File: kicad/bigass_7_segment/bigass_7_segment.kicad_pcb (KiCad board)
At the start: 2 copper layers, 30 x 94 mm, 37 parts, among them J1 Conn_01x02, J2 Conn_01x02, J3 Conn_01x02, J4 Conn_01x02, J5 Conn_01x01, J6 Conn_01x01, J7 Conn_01x01, J8 Conn_01x01, Q3 25V 1.5A

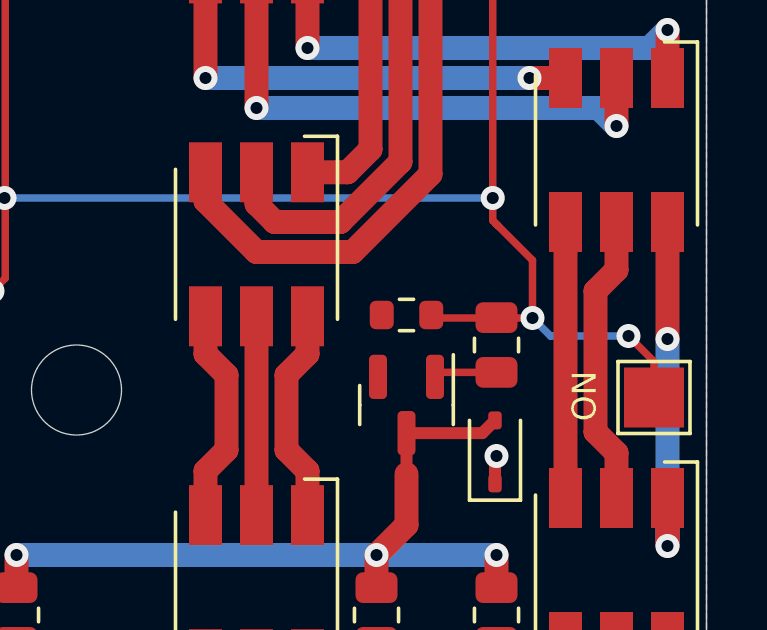
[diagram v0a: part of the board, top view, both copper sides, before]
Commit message: Bigass 7 segment display rev B
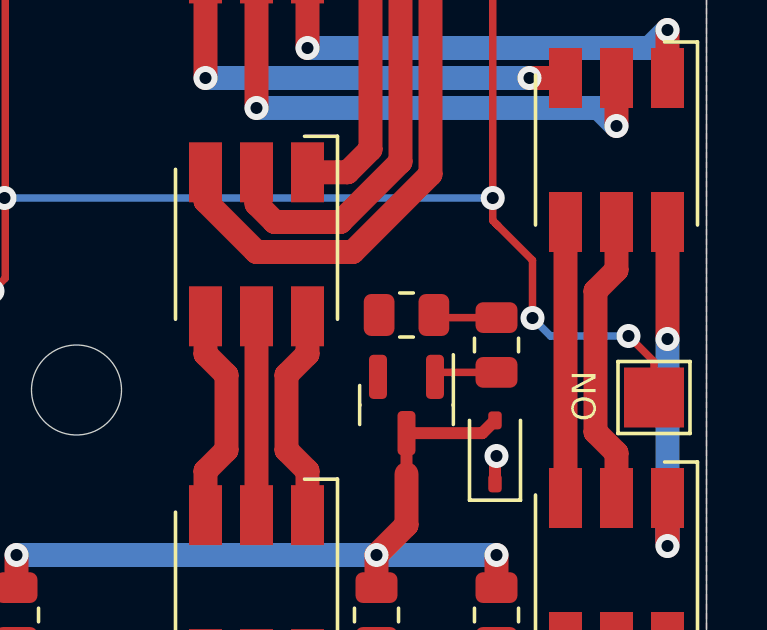
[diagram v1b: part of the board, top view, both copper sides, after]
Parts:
- R1: footprint Resistor_SMD:R_0603_1608Metric -> Resistor_SMD:R_0805_2012Metric
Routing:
- net /LED_ON: track 125.3 -> 123.9 mm

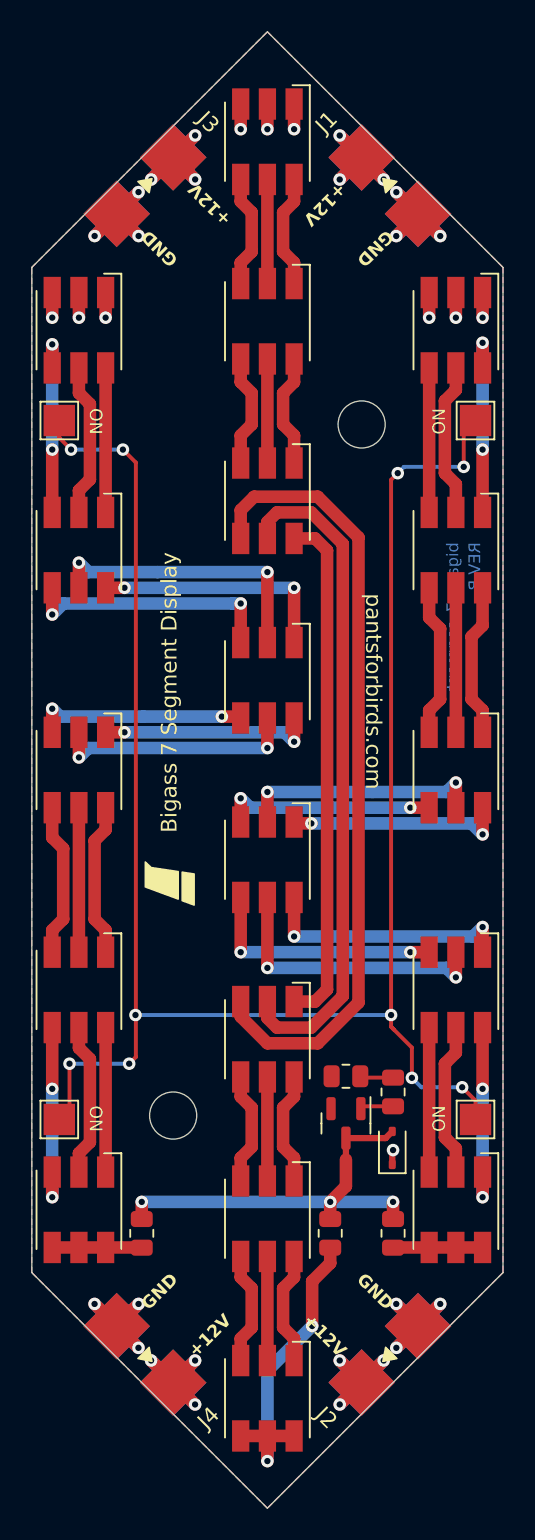
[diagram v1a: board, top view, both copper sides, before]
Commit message: Add demo mode to display code
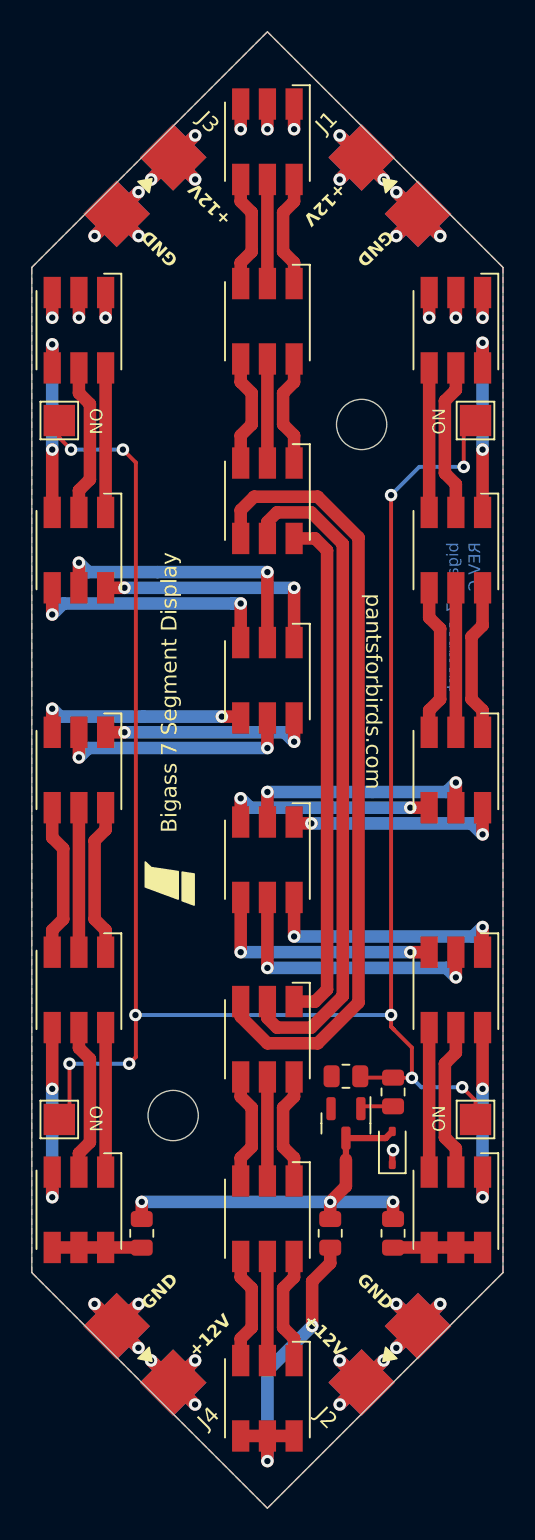
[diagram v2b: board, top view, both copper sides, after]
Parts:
- H1, H2: footprint MountingHole:MountingHole_3mm -> Custom_MountingHole:MountingHole_3.2mm_M3_Isolated
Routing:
- net /LED_ON: track 123.9 -> 124.6 mm
